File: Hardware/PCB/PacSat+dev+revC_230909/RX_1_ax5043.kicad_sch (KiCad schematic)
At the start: 15 parts, among them U151 RFShield_OnePiece, U205 AX5043

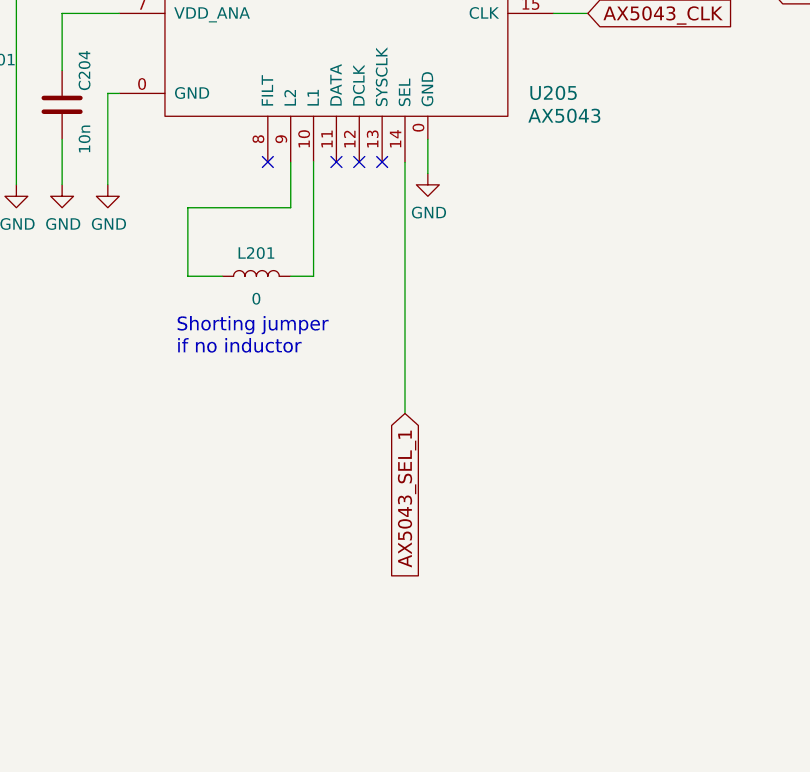
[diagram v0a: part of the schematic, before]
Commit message: Changed schematic to add Select lines for each AX5043 on the CPU.
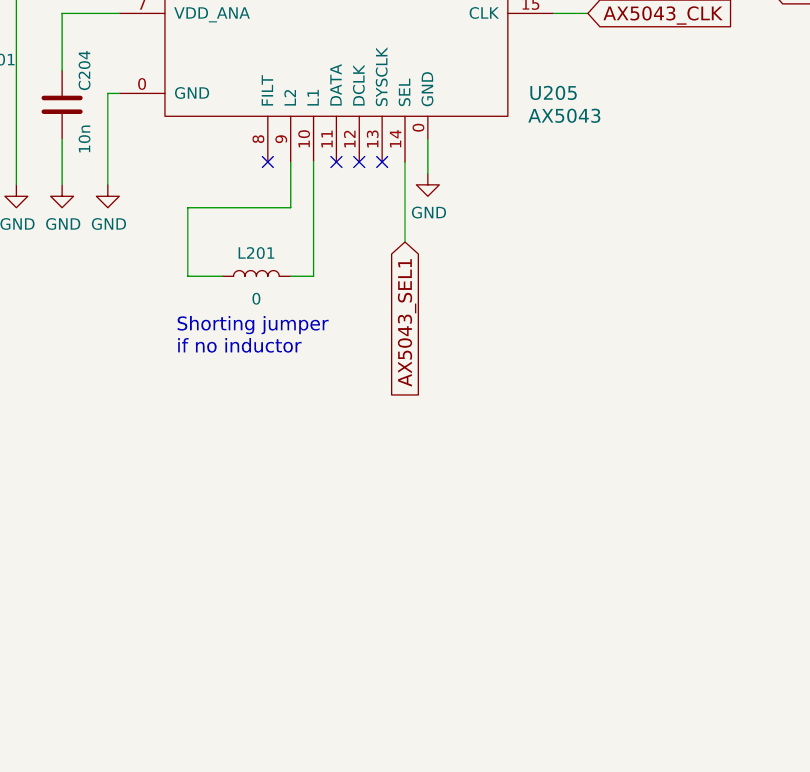
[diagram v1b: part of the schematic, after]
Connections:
- net AX5043_SEL_1 renamed AX5043_SEL1
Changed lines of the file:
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@@
     (stroke (width 0) (type default))
   )
-  (wire (pts (xy 228.6 160.02) (xy 228.6 187.96))
+  (wire (pts (xy 228.6 160.02) (xy 228.6 168.91))
     (stroke (width 0) (type default))
   )
@@
     )
   )
-  (global_label "AX5043_SEL_1" (shape input) (at 228.6 187.96 270) (fields_autoplaced)
+  (global_label "AX5043_SEL1" (shape input) (at 228.6 168.91 270) (fields_autoplaced)
     (effects (font (size 1.524 1.524)) (justify right))
-    (property "Intersheetrefs" "${INTERSHEET_REFS}" (at 228.6 207.0623 90)
+    (property "Intersheetrefs" "${INTERSHEET_REFS}" (at 228.6 186.9466 90)
       (effects (font (size 1.524 1.524)) (justify right) hide)
     )
@@
     (pin "9")
     (instances
-      (project "pACsAT_dEV_rEVc_230907"
+      (project "PacSat+dev+revC_230909"
         (path "/cc9f42d2-6985-41ac-acab-5ab7b01c5b38/07d62cf1-e888-4b13-86c4-67d770627579"
           (reference "U205") (unit 1)
@@
     (pin "2")
     (instances
-      (project "pACsAT_dEV_rEVc_230907"
+      (project "PacSat+dev+revC_230909"
         (path "/cc9f42d2-6985-41ac-acab-5ab7b01c5b38/07d62cf1-e888-4b13-86c4-67d770627579"
           (reference "C204") (unit 1)
@@
     (pin "2")
     (instances
-      (project "pACsAT_dEV_rEVc_230907"
+      (project "PacSat+dev+revC_230909"
         (path "/cc9f42d2-6985-41ac-acab-5ab7b01c5b38/00000000-0000-0000-0000-00005a014be3"
           (reference "C712") (unit 1)
@@
     (pin "2")
     (instances
-      (project "pACsAT_dEV_rEVc_230907"
+      (project "PacSat+dev+revC_230909"
         (path "/cc9f42d2-6985-41ac-acab-5ab7b01c5b38/00000000-0000-0000-0000-00005a014be3"
           (reference "C711") (unit 1)
@@
     (pin "1")
     (instances
-      (project "pACsAT_dEV_rEVc_230907"
+      (project "PacSat+dev+revC_230909"
         (path "/cc9f42d2-6985-41ac-acab-5ab7b01c5b38/07d62cf1-e888-4b13-86c4-67d770627579"
           (reference "#PWR0206") (unit 1)
@@
     (pin "1")
     (instances
-      (project "pACsAT_dEV_rEVc_230907"
+      (project "PacSat+dev+revC_230909"
         (path "/cc9f42d2-6985-41ac-acab-5ab7b01c5b38/00000000-0000-0000-0000-00005a014be3"
           (reference "#PWR0735") (unit 1)
@@
     (pin "1")
     (instances
-      (project "pACsAT_dEV_rEVc_230907"
+      (project "PacSat+dev+revC_230909"
         (path "/cc9f42d2-6985-41ac-acab-5ab7b01c5b38/00000000-0000-0000-0000-00005a014be3"
           (reference "#PWR0161") (unit 1)
@@
     (pin "1")
     (instances
-      (project "pACsAT_dEV_rEVc_230907"
+      (project "PacSat+dev+revC_230909"
         (path "/cc9f42d2-6985-41ac-acab-5ab7b01c5b38/07d62cf1-e888-4b13-86c4-67d770627579"
           (reference "#PWR0211") (unit 1)
@@
     (pin "1")
     (instances
-      (project "pACsAT_dEV_rEVc_230907"
+      (project "PacSat+dev+revC_230909"
         (path "/cc9f42d2-6985-41ac-acab-5ab7b01c5b38/07d62cf1-e888-4b13-86c4-67d770627579"
           (reference "#PWR0205") (unit 1)
@@
     (pin "1")
     (instances
-      (project "pACsAT_dEV_rEVc_230907"
+      (project "PacSat+dev+revC_230909"
         (path "/cc9f42d2-6985-41ac-acab-5ab7b01c5b38/00000000-0000-0000-0000-00005a014be3"
           (reference "#PWR0161") (unit 1)
@@
     (pin "2")
     (instances
-      (project "pACsAT_dEV_rEVc_230907"
+      (project "PacSat+dev+revC_230909"
         (path "/cc9f42d2-6985-41ac-acab-5ab7b01c5b38/07d62cf1-e888-4b13-86c4-67d770627579"
           (reference "C207") (unit 1)
@@
     (pin "2")
     (instances
-      (project "pACsAT_dEV_rEVc_230907"
+      (project "PacSat+dev+revC_230909"
         (path "/cc9f42d2-6985-41ac-acab-5ab7b01c5b38/07d62cf1-e888-4b13-86c4-67d770627579"
           (reference "C203") (unit 1)
@@
     (pin "1")
     (instances
-      (project "pACsAT_dEV_rEVc_230907"
+      (project "PacSat+dev+revC_230909"
         (path "/cc9f42d2-6985-41ac-acab-5ab7b01c5b38/00000000-0000-0000-0000-00005a014be3"
           (reference "#PWR0161") (unit 1)
@@
     (pin "1")
     (instances
-      (project "pACsAT_dEV_rEVc_230907"
+      (project "PacSat+dev+revC_230909"
         (path "/cc9f42d2-6985-41ac-acab-5ab7b01c5b38/00000000-0000-0000-0000-00005a014be3"
           (reference "#PWR0161") (unit 1)
@@
     (pin "1")
     (instances
-      (project "pACsAT_dEV_rEVc_230907"
+      (project "PacSat+dev+revC_230909"
         (path "/cc9f42d2-6985-41ac-acab-5ab7b01c5b38/9af0eacb-5211-4e23-85d7-9c1805bbe6a4"
           (reference "#PWR0614") (unit 1)
@@
     (pin "1")
     (instances
-      (project "pACsAT_dEV_rEVc_230907"
+      (project "PacSat+dev+revC_230909"
         (path "/cc9f42d2-6985-41ac-acab-5ab7b01c5b38/07d62cf1-e888-4b13-86c4-67d770627579"
           (reference "#PWR0210") (unit 1)
@@
     (pin "1")
     (instances
-      (project "pACsAT_dEV_rEVc_230907"
+      (project "PacSat+dev+revC_230909"
         (path "/cc9f42d2-6985-41ac-acab-5ab7b01c5b38/07d62cf1-e888-4b13-86c4-67d770627579"
           (reference "#PWR0212") (unit 1)
@@
     (pin "2")
     (instances
-      (project "pACsAT_dEV_rEVc_230907"
+      (project "PacSat+dev+revC_230909"
         (path "/cc9f42d2-6985-41ac-acab-5ab7b01c5b38/07d62cf1-e888-4b13-86c4-67d770627579"
           (reference "C201") (unit 1)
@@
     (pin "2")
     (instances
-      (project "pACsAT_dEV_rEVc_230907"
+      (project "PacSat+dev+revC_230909"
         (path "/cc9f42d2-6985-41ac-acab-5ab7b01c5b38/07d62cf1-e888-4b13-86c4-67d770627579"
           (reference "L201") (unit 1)
@@
     (pin "1")
     (instances
-      (project "pACsAT_dEV_rEVc_230907"
+      (project "PacSat+dev+revC_230909"
         (path "/cc9f42d2-6985-41ac-acab-5ab7b01c5b38/00000000-0000-0000-0000-00005a014be3"
           (reference "#PWR0161") (unit 1)
@@
     (pin "1")
     (instances
-      (project "pACsAT_dEV_rEVc_230907"
+      (project "PacSat+dev+revC_230909"
         (path "/cc9f42d2-6985-41ac-acab-5ab7b01c5b38/07d62cf1-e888-4b13-86c4-67d770627579"
           (reference "#PWR0209") (unit 1)
@@
     (pin "3")
     (instances
-      (project "pACsAT_dEV_rEVc_230907"
+      (project "PacSat+dev+revC_230909"
         (path "/cc9f42d2-6985-41ac-acab-5ab7b01c5b38/9af0eacb-5211-4e23-85d7-9c1805bbe6a4"
           (reference "U605") (unit 1)
@@
     (pin "1")
     (instances
-      (project "pACsAT_dEV_rEVc_230907"
+      (project "PacSat+dev+revC_230909"
         (path "/cc9f42d2-6985-41ac-acab-5ab7b01c5b38/07d62cf1-e888-4b13-86c4-67d770627579"
           (reference "#PWR0204") (unit 1)
@@
     (pin "1")
     (instances
-      (project "pACsAT_dEV_rEVc_230907"
+      (project "PacSat+dev+revC_230909"
         (path "/cc9f42d2-6985-41ac-acab-5ab7b01c5b38/07d62cf1-e888-4b13-86c4-67d770627579"
           (reference "#PWR0203") (unit 1)
@@
     (pin "2")
     (instances
-      (project "pACsAT_dEV_rEVc_230907"
+      (project "PacSat+dev+revC_230909"
         (path "/cc9f42d2-6985-41ac-acab-5ab7b01c5b38/07d62cf1-e888-4b13-86c4-67d770627579"
           (reference "R202") (unit 1)
@@
     (pin "2")
     (instances
-      (project "pACsAT_dEV_rEVc_230907"
+      (project "PacSat+dev+revC_230909"
         (path "/cc9f42d2-6985-41ac-acab-5ab7b01c5b38/07d62cf1-e888-4b13-86c4-67d770627579"
           (reference "C202") (unit 1)
@@
     (pin "5")
     (instances
-      (project "pACsAT_dEV_rEVc_230907"
+      (project "PacSat+dev+revC_230909"
         (path "/cc9f42d2-6985-41ac-acab-5ab7b01c5b38/00000000-0000-0000-0000-00005a014be3"
           (reference "U151") (unit 1)
@@
     (pin "2")
     (instances
-      (project "pACsAT_dEV_rEVc_230907"
+      (project "PacSat+dev+revC_230909"
         (path "/cc9f42d2-6985-41ac-acab-5ab7b01c5b38/07d62cf1-e888-4b13-86c4-67d770627579"
           (reference "R201") (unit 1)
@@
     (pin "1")
     (instances
-      (project "pACsAT_dEV_rEVc_230907"
+      (project "PacSat+dev+revC_230909"
         (path "/cc9f42d2-6985-41ac-acab-5ab7b01c5b38/07d62cf1-e888-4b13-86c4-67d770627579"
           (reference "#PWR0208") (unit 1)
@@
     (pin "2")
     (instances
-      (project "pACsAT_dEV_rEVc_230907"
+      (project "PacSat+dev+revC_230909"
         (path "/cc9f42d2-6985-41ac-acab-5ab7b01c5b38/07d62cf1-e888-4b13-86c4-67d770627579"
           (reference "R203") (unit 1)
@@
     (pin "3")
     (instances
-      (project "pACsAT_dEV_rEVc_230907"
+      (project "PacSat+dev+revC_230909"
         (path "/cc9f42d2-6985-41ac-acab-5ab7b01c5b38/9af0eacb-5211-4e23-85d7-9c1805bbe6a4"
           (reference "U607") (unit 1)
